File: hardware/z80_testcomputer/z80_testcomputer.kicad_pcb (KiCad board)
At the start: 2 copper layers, 95 x 100 mm, 7 parts

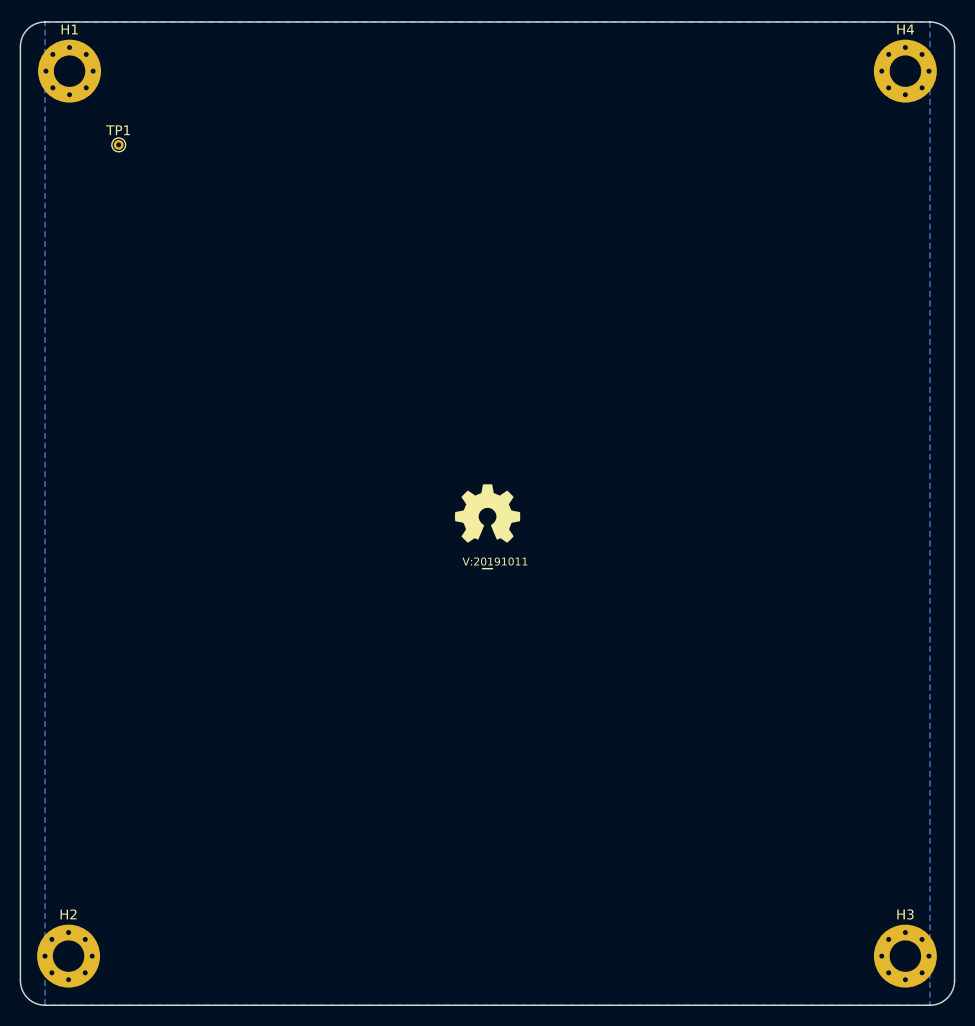
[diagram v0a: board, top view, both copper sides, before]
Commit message: changed mounting holes
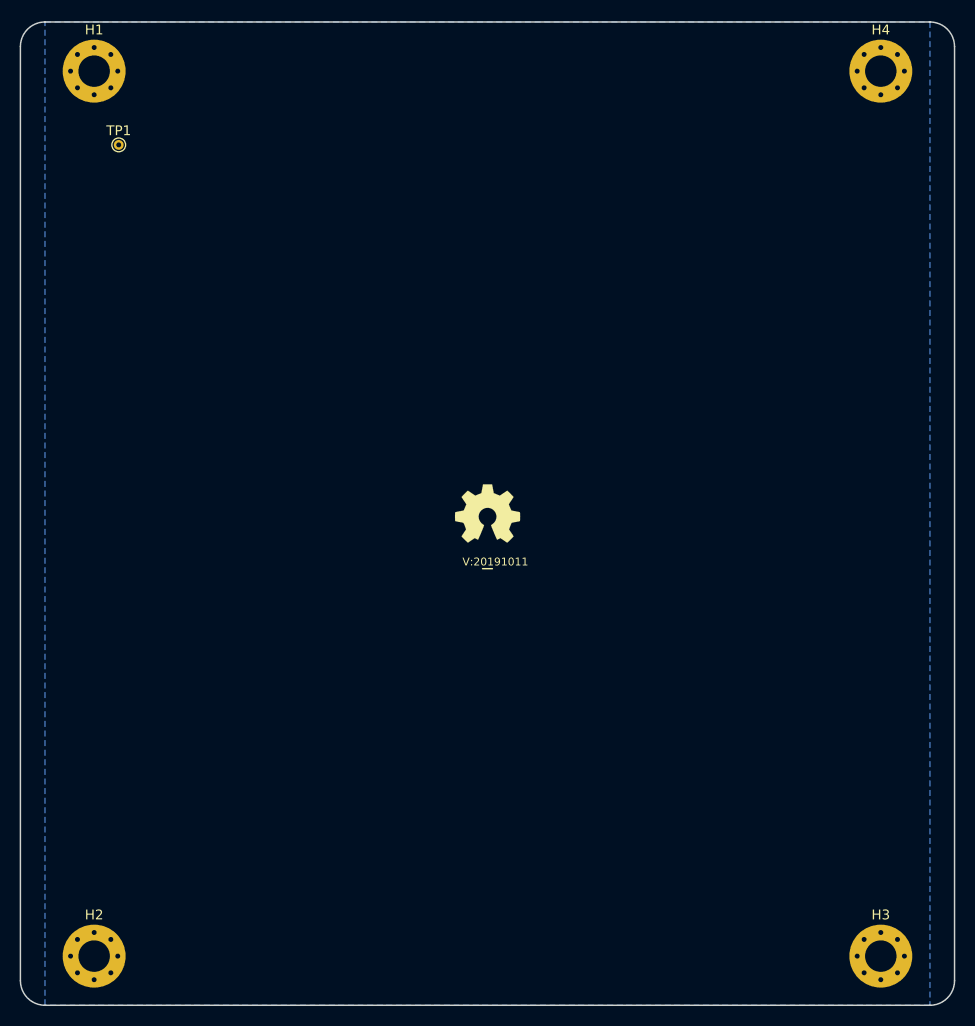
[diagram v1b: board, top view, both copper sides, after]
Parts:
- moved H2 2.60 mm to (110.0, 145.0)
- moved H1 2.50 mm to (110.0, 55.0)
- moved H3 2.50 mm to (190.0, 145.0)
- moved H4 2.50 mm to (190.0, 55.0)
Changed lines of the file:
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@@
   )
   (module MountingHole:MountingHole_3.2mm_M3_Pad_Via (layer F.Cu)
-    (at 192.5 55)
+    (at 190 55)
     (descr "Mounting Hole 3.2mm, M3")
     (tags "mounting hole 3.2mm m3")
@@
   )
   (module MountingHole:MountingHole_3.2mm_M3_Pad_Via (layer F.Cu)
-    (at 192.5 145)
+    (at 190 145)
     (descr "Mounting Hole 3.2mm, M3")
     (tags "mounting hole 3.2mm m3")
@@
   )
   (module MountingHole:MountingHole_3.2mm_M3_Pad_Via (layer F.Cu)
-    (at 107.4 145)
+    (at 110 145)
     (descr "Mounting Hole 3.2mm, M3")
     (tags "mounting hole 3.2mm m3")
@@
   )
   (module MountingHole:MountingHole_3.2mm_M3_Pad_Via (layer F.Cu)
-    (at 107.5 55)
+    (at 110 55)
     (descr "Mounting Hole 3.2mm, M3")
     (tags "mounting hole 3.2mm m3")

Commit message: added bus
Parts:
- added J1: Conn_02x15_Odd_Even, Connector_PinHeader_2.54mm:PinHeader_2x15_P2.54mm_Vertical, F.Cu at (187.3, 61.6)
- added J2: Conn_02x15_Odd_Even, Connector_PinHeader_2.54mm:PinHeader_2x15_P2.54mm_Vertical, F.Cu at (187.3, 102.2)
- added TP2: testpad, TestPoint:TestPoint_THTPad_D1.0mm_Drill0.5mm, F.Cu at (121.3, 55.9)
- moved TP1 8.79 mm to (121.3, 62.2)
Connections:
- TP1 pad 1: (no net) -> /VSS
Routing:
- net /VSS: track 0.00 -> 131.6 mm
- net /VDD: track 0.00 -> 52.0 mm
- removed copper zone on B.Cu, net /VSS

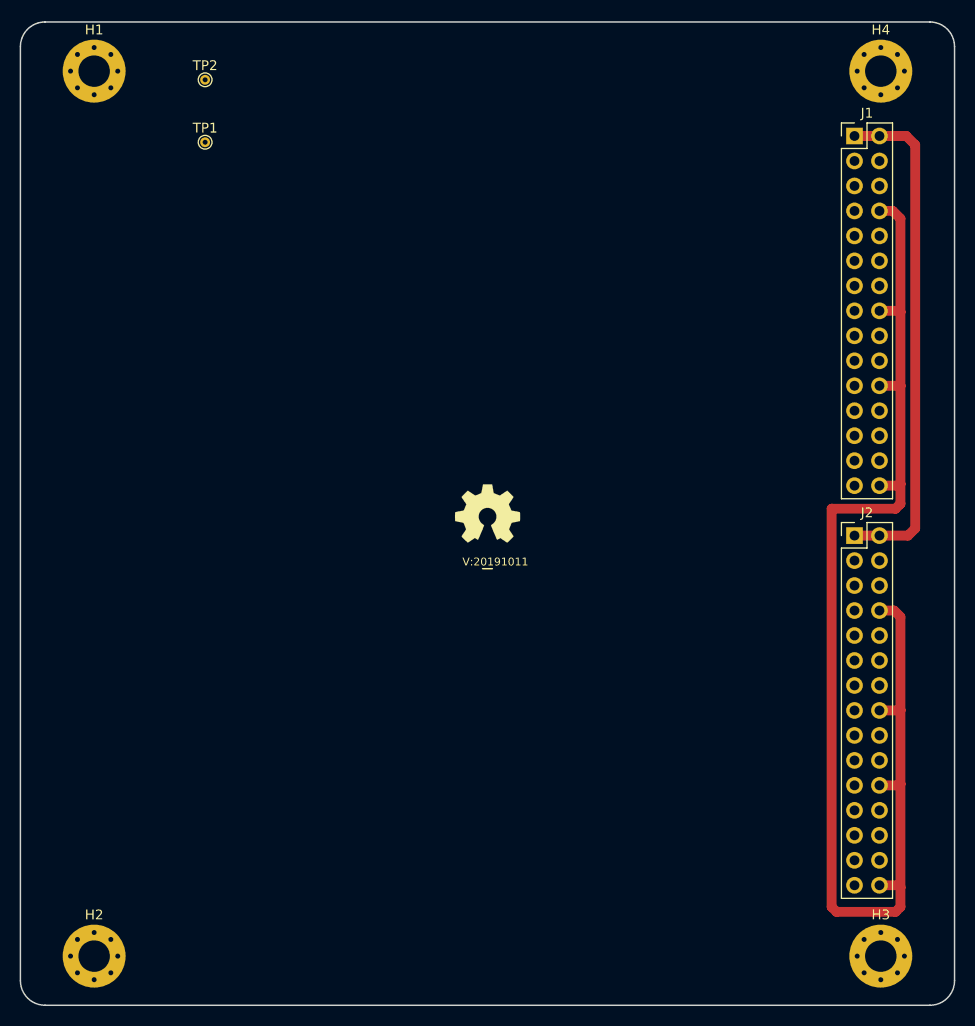
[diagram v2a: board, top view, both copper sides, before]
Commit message: added z80 cpu, modified interface bus pinning
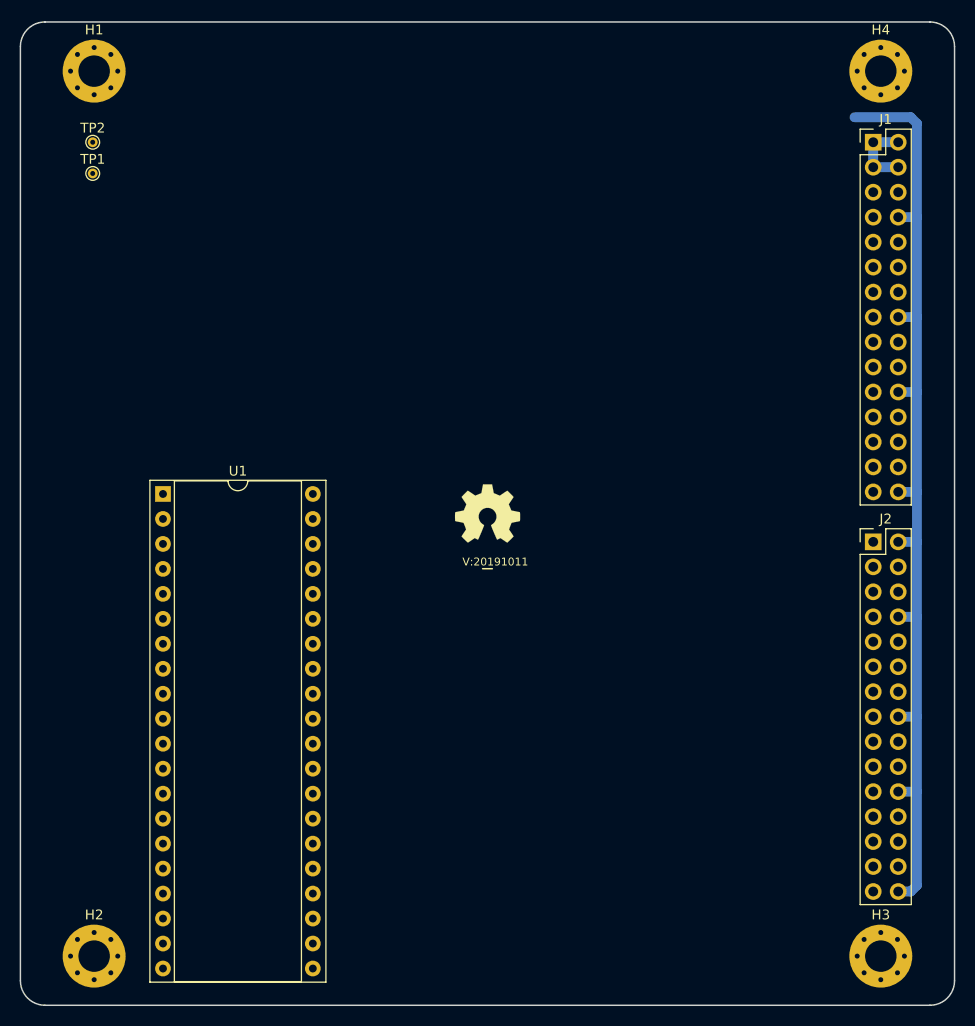
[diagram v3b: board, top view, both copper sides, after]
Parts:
- added U1: Z84C000XPEG, Package_DIP:DIP-40_W15.24mm_Socket, F.Cu at (117.0, 98.0)
- moved TP2 13.1 mm to (109.9, 62.2)
- moved TP1 11.9 mm to (109.9, 65.4)
- moved J2 2.01 mm to (189.2, 102.9)
- moved J1 2.01 mm to (189.2, 62.2)
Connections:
- J1 pad 3: (no net) -> /VDD
- J1 pad 4: (no net) -> /VDD
- J2 pad 1: /VDD -> (no net)
- J2 pad 2: /VDD -> /VSS
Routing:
- net /VDD: track 52.0 -> 7.62 mm
- net /VSS: track 131.6 -> 101.5 mm

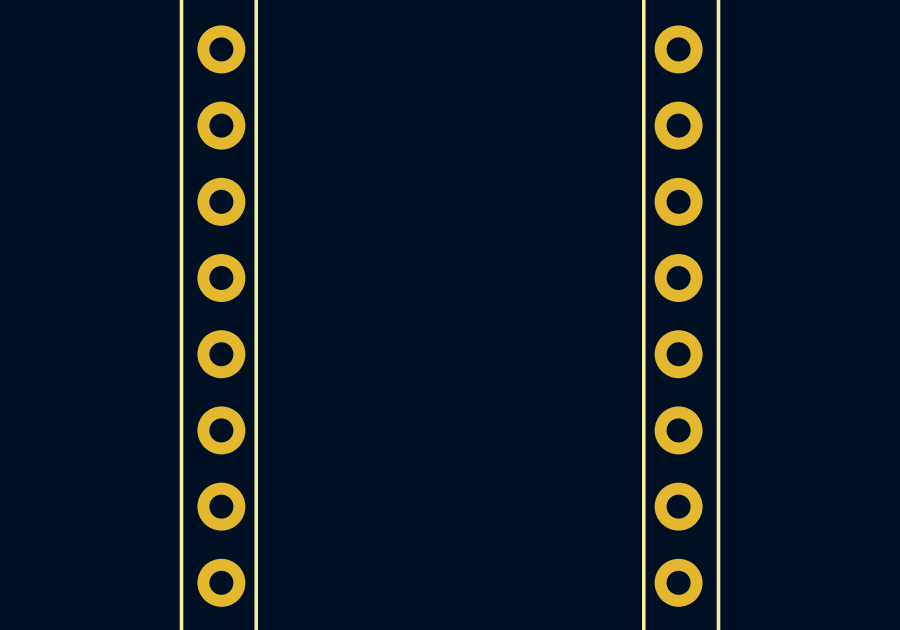
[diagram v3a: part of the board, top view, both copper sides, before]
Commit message: added decoupling for Z80 CPU
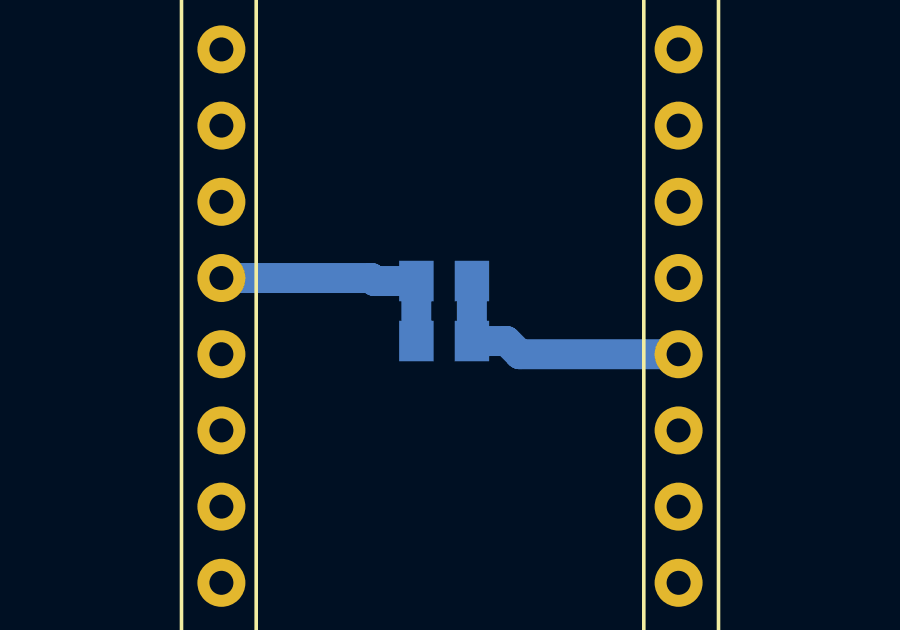
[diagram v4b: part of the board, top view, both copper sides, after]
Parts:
- added C1: 100n, SquantorRcl:C_0805+0603, B.Cu at (124.4, 125.5)
- added C2: 1u, SquantorRcl:C_0805+0603, B.Cu at (124.4, 123.5)
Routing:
- net /VSS: track 101.5 -> 110.6 mm
- net /VDD: track 7.62 -> 16.2 mm
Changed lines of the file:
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@@
     (thickness 1.6)
     (drawings 10)
-    (tracks 24)
+    (tracks 32)
     (zones 0)
-    (modules 11)
+    (modules 13)
     (nets 3)
   )
@@
     (add_net "Net-(J2-Pad9)")
   )
+  (module SquantorRcl:C_0805+0603 (layer B.Cu)
+    (at 124.425 123.5 180)
+    (descr "Capacitor SMD 0805 and 0603 pad sizes, reflow soldering, based on AVX dimensions")
+    (tags "capacitor 0805 0603 mixed")
+    (attr smd)
+    (fp_text reference C2 (at 0 2.1) (layer B.SilkS)
+      (effects (font (size 1 1) (thickness 0.15)) (justify mirror))
+    )
+    (fp_text value 1u (at 0 -2.1) (layer B.Fab)
+      (effects (font (size 1 1) (thickness 0.15)) (justify mirror))
+    )
+    (fp_line (start 0 0.6) (end 0 -0.6) (layer B.SilkS) (width 0.15))
+    (fp_line (start -0.9 -0.625) (end -0.9 0.625) (layer B.Fab) (width 0.1))
+    (fp_line (start 0.9 -0.625) (end -0.9 -0.625) (layer B.Fab) (width 0.1))
+    (fp_line (start 0.9 0.625) (end 0.9 -0.625) (layer B.Fab) (width 0.1))
+    (fp_line (start -0.9 0.625) (end 0.9 0.625) (layer B.Fab) (width 0.1))
+    (fp_line (start -1.75 0.95) (end 1.75 0.95) (layer B.CrtYd) (width 0.05))
+    (fp_line (start -1.75 -0.95) (end 1.75 -0.95) (layer B.CrtYd) (width 0.05))
+    (fp_line (start -1.75 0.95) (end -1.75 -0.95) (layer B.CrtYd) (width 0.05))
+    (fp_line (start 1.75 0.95) (end 1.75 -0.95) (layer B.CrtYd) (width 0.05))
+    (pad 1 smd rect (at -0.925 0 180) (size 1.15 1.35) (layers B.Cu B.Paste B.Mask)
+      (net 1 /VSS))
+    (pad 2 smd rect (at 0.925 0 180) (size 1.15 1.35) (layers B.Cu B.Paste B.Mask)
+      (net 2 /VDD))
+    (model ${KISYS3DMOD}/Capacitor_SMD.3dshapes/C_0805_2012Metric.step
+      (at (xyz 0 0 0))
+      (scale (xyz 1 1 1))
+      (rotate (xyz 0 0 0))
+    )
+  )
+  (module SquantorRcl:C_0805+0603 (layer B.Cu)
+    (at 124.425 125.5 180)
+    (descr "Capacitor SMD 0805 and 0603 pad sizes, reflow soldering, based on AVX dimensions")
+    (tags "capacitor 0805 0603 mixed")
+    (attr smd)
+    (fp_text reference C1 (at 0 2.1) (layer B.SilkS)
+      (effects (font (size 1 1) (thickness 0.15)) (justify mirror))
+    )
+    (fp_text value 100n (at 0 -2.1) (layer B.Fab)
+      (effects (font (size 1 1) (thickness 0.15)) (justify mirror))
+    )
+    (fp_line (start 0 0.6) (end 0 -0.6) (layer B.SilkS) (width 0.15))
+    (fp_line (start -0.9 -0.625) (end -0.9 0.625) (layer B.Fab) (width 0.1))
+    (fp_line (start 0.9 -0.625) (end -0.9 -0.625) (layer B.Fab) (width 0.1))
+    (fp_line (start 0.9 0.625) (end 0.9 -0.625) (layer B.Fab) (width 0.1))
+    (fp_line (start -0.9 0.625) (end 0.9 0.625) (layer B.Fab) (width 0.1))
+    (fp_line (start -1.75 0.95) (end 1.75 0.95) (layer B.CrtYd) (width 0.05))
+    (fp_line (start -1.75 -0.95) (end 1.75 -0.95) (layer B.CrtYd) (width 0.05))
+    (fp_line (start -1.75 0.95) (end -1.75 -0.95) (layer B.CrtYd) (width 0.05))
+    (fp_line (start 1.75 0.95) (end 1.75 -0.95) (layer B.CrtYd) (width 0.05))
+    (pad 1 smd rect (at -0.925 0 180) (size 1.15 1.35) (layers B.Cu B.Paste B.Mask)
+      (net 1 /VSS))
+    (pad 2 smd rect (at 0.925 0 180) (size 1.15 1.35) (layers B.Cu B.Paste B.Mask)
+      (net 2 /VDD))
+    (model ${KISYS3DMOD}/Capacitor_SMD.3dshapes/C_0805_2012Metric.step
+      (at (xyz 0 0 0))
+      (scale (xyz 1 1 1))
+      (rotate (xyz 0 0 0))
+    )
+  )
   (module Package_DIP:DIP-40_W15.24mm_Socket (layer F.Cu)
     (at 117 98)
@@
   (segment (start 193.675 128.27) (end 193.675 120.65) (width 1) (layer B.Cu) (net 1))
   (segment (start 193.675 120.65) (end 193.675 110.49) (width 1) (layer B.Cu) (net 1))
+  (segment (start 125.35 125.5) (end 126.5 125.5) (width 1) (layer B.Cu) (net 1))
+  (segment (start 126.94 125.94) (end 132.24 125.94) (width 1) (layer B.Cu) (net 1))
+  (segment (start 126.5 125.5) (end 126.94 125.94) (width 1) (layer B.Cu) (net 1))
+  (segment (start 125.35 125.5) (end 125.35 123.5) (width 1) (layer B.Cu) (net 1))
   (segment (start 189.23 62.23) (end 189.23 64.77) (width 1) (layer B.Cu) (net 2))
   (segment (start 189.23 64.77) (end 191.77 64.77) (width 1) (layer B.Cu) (net 2))
   (segment (start 189.23 62.23) (end 191.77 62.23) (width 1) (layer B.Cu) (net 2))
+  (segment (start 122.1 123.5) (end 123.5 123.5) (width 1) (layer B.Cu) (net 2))
+  (segment (start 117 123.4) (end 122 123.4) (width 1) (layer B.Cu) (net 2))
+  (segment (start 122 123.4) (end 122.1 123.5) (width 1) (layer B.Cu) (net 2))
+  (segment (start 123.5 125.5) (end 123.5 123.5) (width 1) (layer B.Cu) (net 2))
   (zone (net 0) (net_name "") (layers F&B.Cu) (hatch edge 0.508)
     (connect_pads (clearance 0.508))
